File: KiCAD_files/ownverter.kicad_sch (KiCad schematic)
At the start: 11 parts, among them J101 Harting-15 and Wago 6

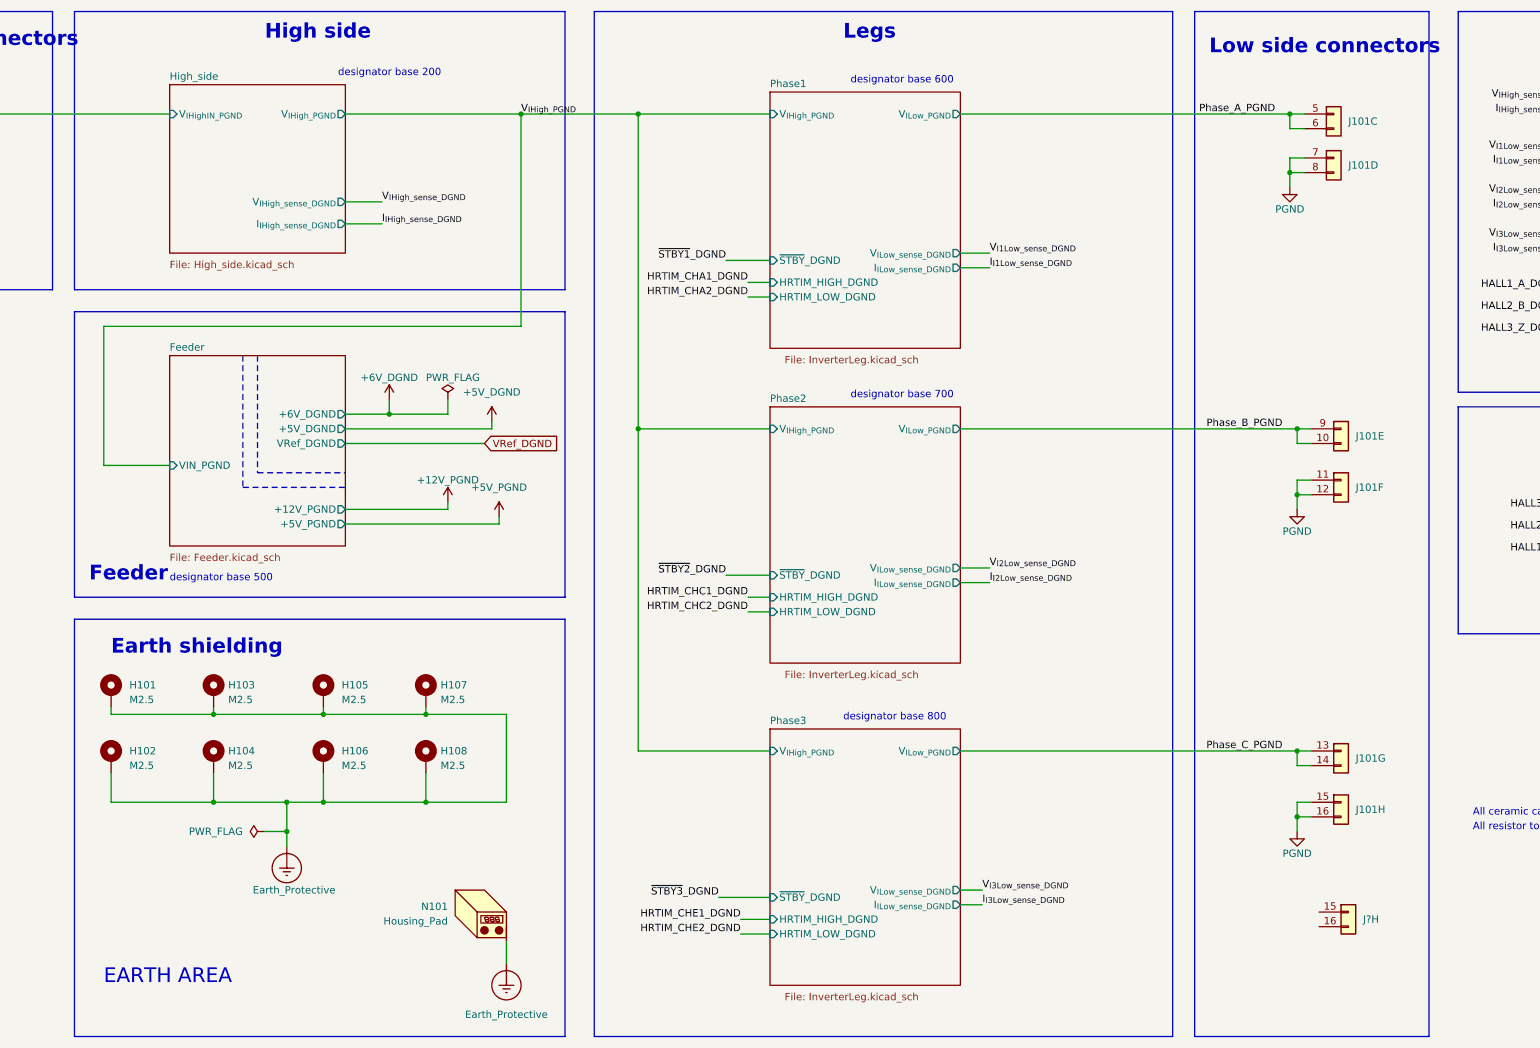
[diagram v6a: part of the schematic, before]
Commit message: correct datasheet link
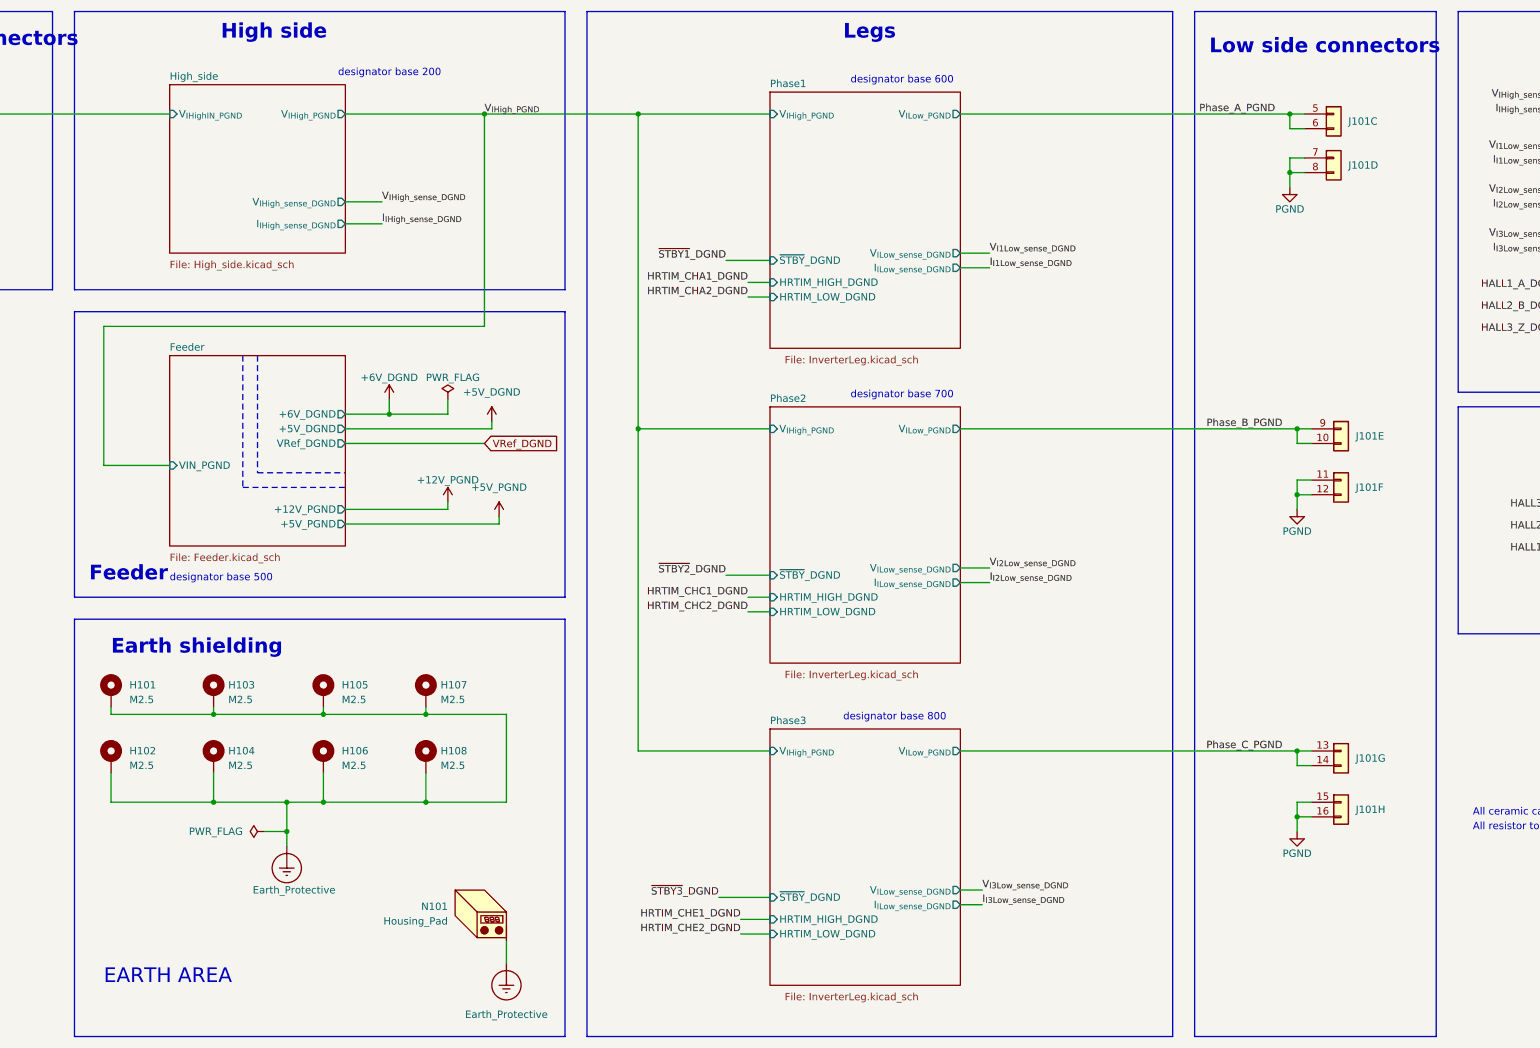
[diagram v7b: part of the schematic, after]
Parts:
- removed J?: Harting-15 and Wago 6, Footprints:Harting - 15contacts and Wago, symbol Symbols:Harting 15 contacts and WAGO
